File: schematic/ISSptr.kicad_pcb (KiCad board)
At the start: 2 copper layers, 31 parts, among them J1 TYPE-C-31-M-12, J2 PROG, J3 B5B-XH-A, J4 Servo, Q1 BC817, Q2 BC817, U1 AMS1117-3.3, U2 ESP-WROOM-32, U3 HMC5883L-TR, U4 ULN2003AD

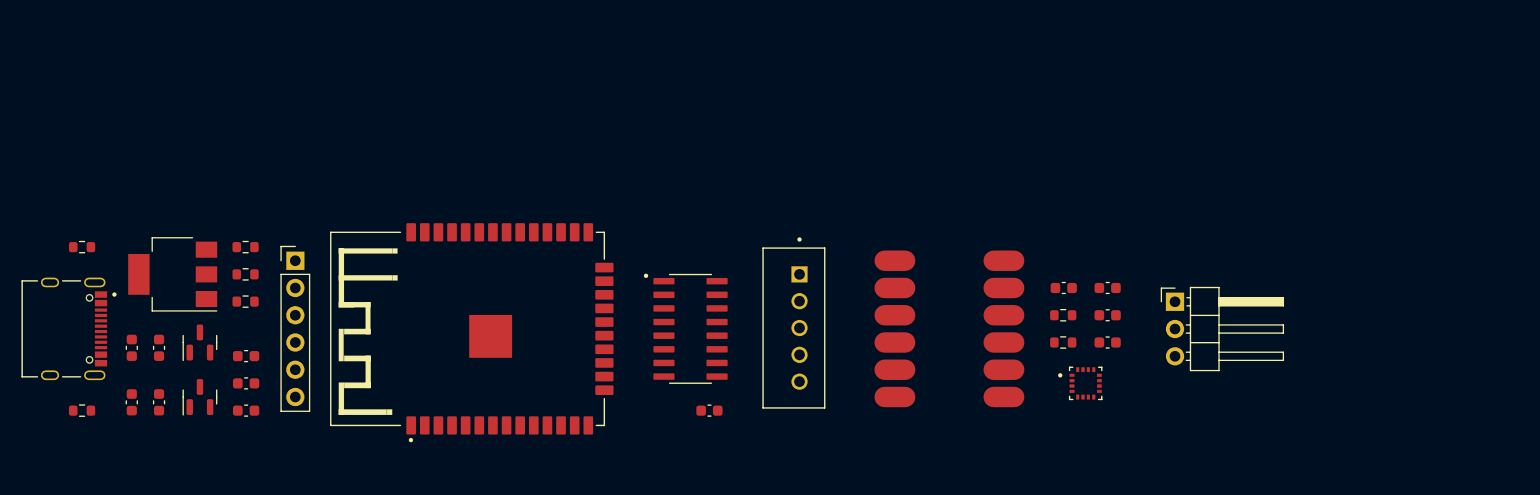
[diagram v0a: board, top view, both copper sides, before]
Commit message: Remove component outlines on silkscreen
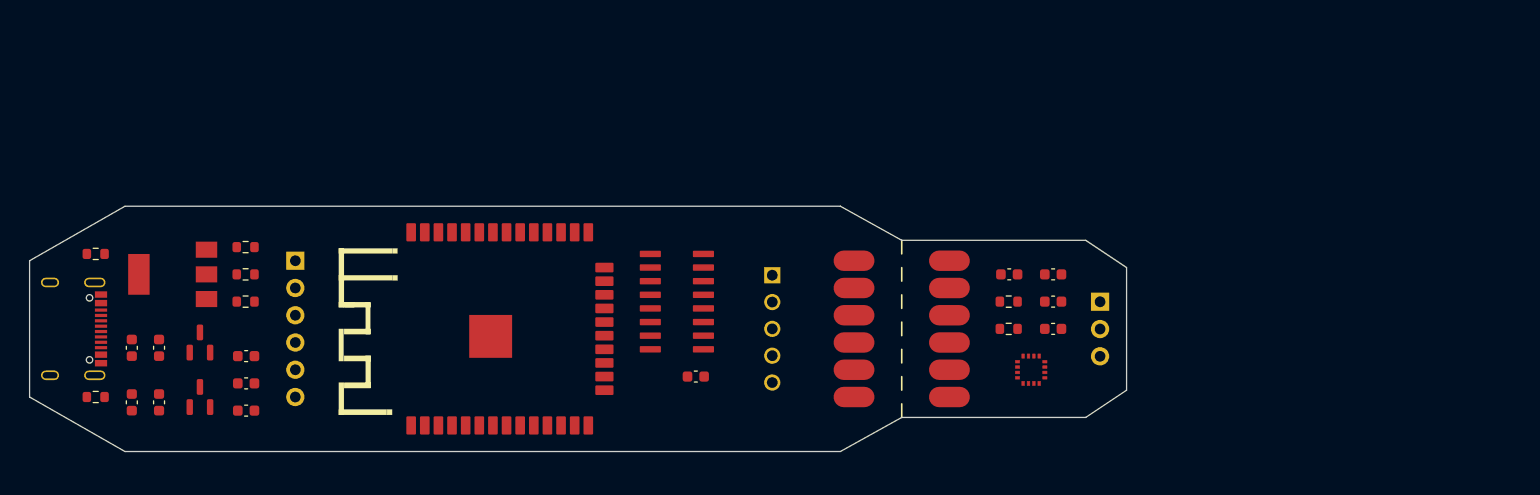
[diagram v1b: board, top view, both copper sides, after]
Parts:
- moved J4 6.98 mm to (157.6, 99.1)
- moved R7 5.24 mm to (149.0, 101.6)
- moved U3 5.24 mm to (151.1, 105.4)
- moved R6 5.24 mm to (149.0, 99.1)
- moved C10 5.24 mm to (153.2, 101.6)
- moved C11 5.24 mm to (149.1, 96.5)
- moved C8 5.24 mm to (153.2, 96.5)
- moved C9 5.24 mm to (153.2, 99.1)
- moved J6 5.08 mm to (143.5, 101.6)
- moved J5 3.81 mm to (134.6, 101.6)
- moved C12 3.42 mm to (119.9, 106.0)
- moved U4 2.84 mm to (118.1, 99.1)
- moved J3 2.54 mm to (126.5, 101.6)
- moved R2 1.80 mm to (63.9, 108.0)
- moved R1 1.42 mm to (63.9, 94.6)
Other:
- board outline added: 102.2 x 22.9 mm

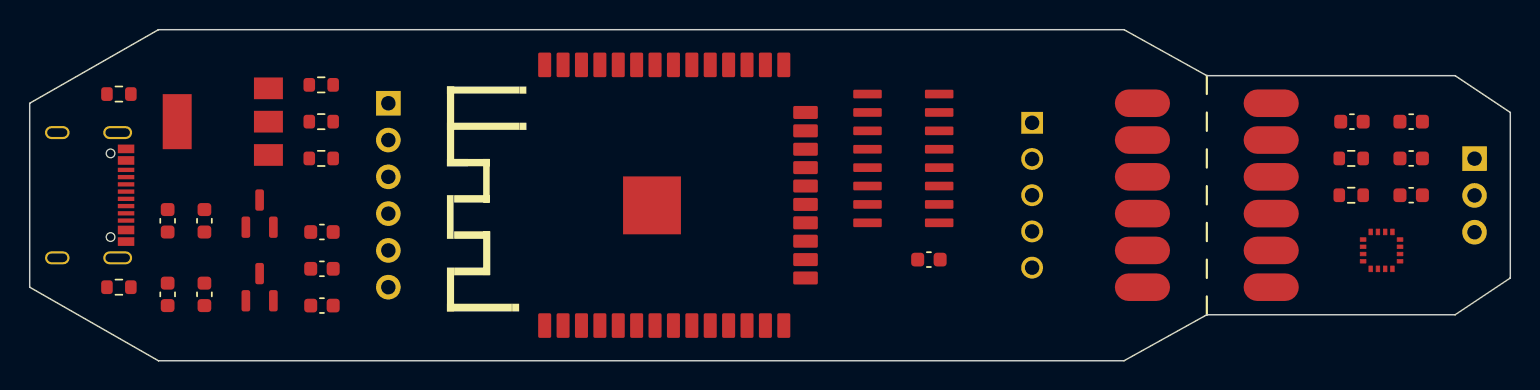
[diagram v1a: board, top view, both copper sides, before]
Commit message: Trace PCB
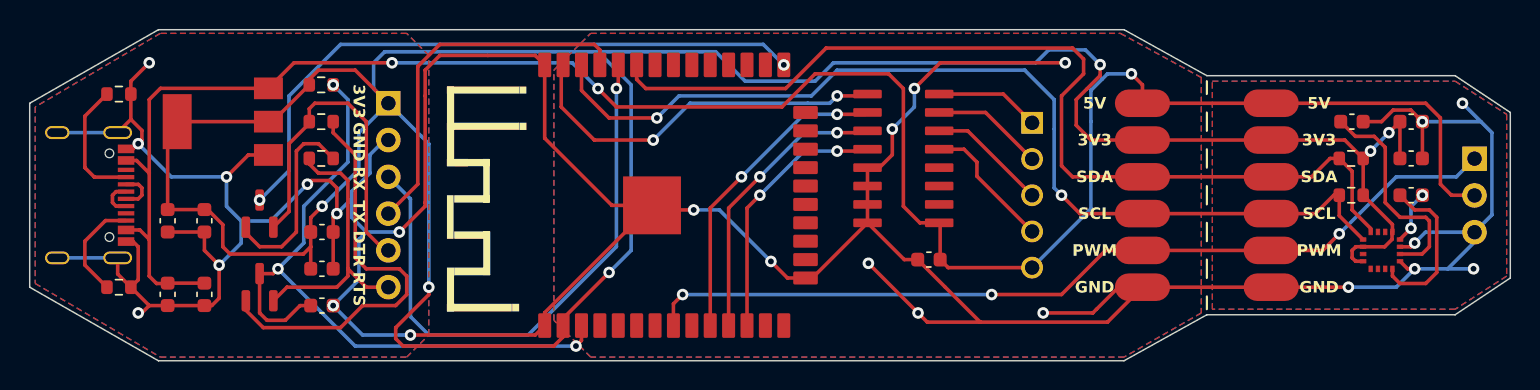
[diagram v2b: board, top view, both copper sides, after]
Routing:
- net GND: track 0.00 -> 286.1 mm, vias 0 -> 24
- net +3.3V: track 0.00 -> 200.9 mm, vias 0 -> 6
- net +5V: track 0.00 -> 143.8 mm, vias 0 -> 3
- net /Compass/SCL: track 0.00 -> 68.2 mm, vias 0 -> 2
- net /Compass/SDA: track 0.00 -> 67.6 mm
- net /ESP32/SERVO: track 0.00 -> 61.0 mm, vias 0 -> 3
- net Net-(Q1-C): track 0.00 -> 47.8 mm, vias 0 -> 3
- net Net-(Q2-C): track 0.00 -> 44.3 mm, vias 0 -> 2
- net /ESP32/PROG_RX: track 0.00 -> 40.2 mm, vias 0 -> 1
- net Net-(Q1-B): track 0.00 -> 28.6 mm
- net /ESP32/STEPPER_A: track 0.00 -> 26.4 mm, vias 0 -> 2
- net /ESP32/PROG_TX: track 0.00 -> 25.4 mm
- net /ESP32/PROG_DTR: track 0.00 -> 23.5 mm
- net /ESP32/STEPPER_B: track 0.00 -> 21.7 mm, vias 0 -> 2
- net /ESP32/STEPPER_C: track 0.00 -> 19.9 mm, vias 0 -> 2
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- added copper zone on B.Cu, net GND
- added copper zone on F.Cu, net GND
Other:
- board text added: "3V3"
- board text added: "5V"
- board text added: "DTR"
- board text added: "GND"
- board text added: "PWM"
- board text added: "RTS"
- board text added: "RX"
- board text added: "SCL"
- board text added: "SDA"
- board text added: "TX"
- board text added: "made with <3 in prague"

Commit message: Setup PCB for production
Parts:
- moved C11 32.6 mm to (181.7, 96.5)
- moved C12 32.6 mm to (152.5, 106.0)
- moved C2 32.6 mm to (102.4, 108.4)
- moved C3 32.6 mm to (102.4, 103.4)
- moved J1 32.6 mm to (92.3, 101.6)
- moved J2 32.6 mm to (115.1, 95.2)
- moved J3 32.6 mm to (159.1, 101.6)
- moved J5 32.6 mm to (167.2, 101.6)
- moved J6 32.6 mm to (176.1, 101.6)
- moved Q1 32.6 mm to (106.2, 108.0)
- moved Q2 32.6 mm to (106.2, 102.9)
- moved R6 32.6 mm to (181.6, 99.1)
- moved R7 32.6 mm to (181.6, 101.6)
- moved U2 32.6 mm to (134.2, 101.6)
- moved U3 32.6 mm to (183.7, 105.4)
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
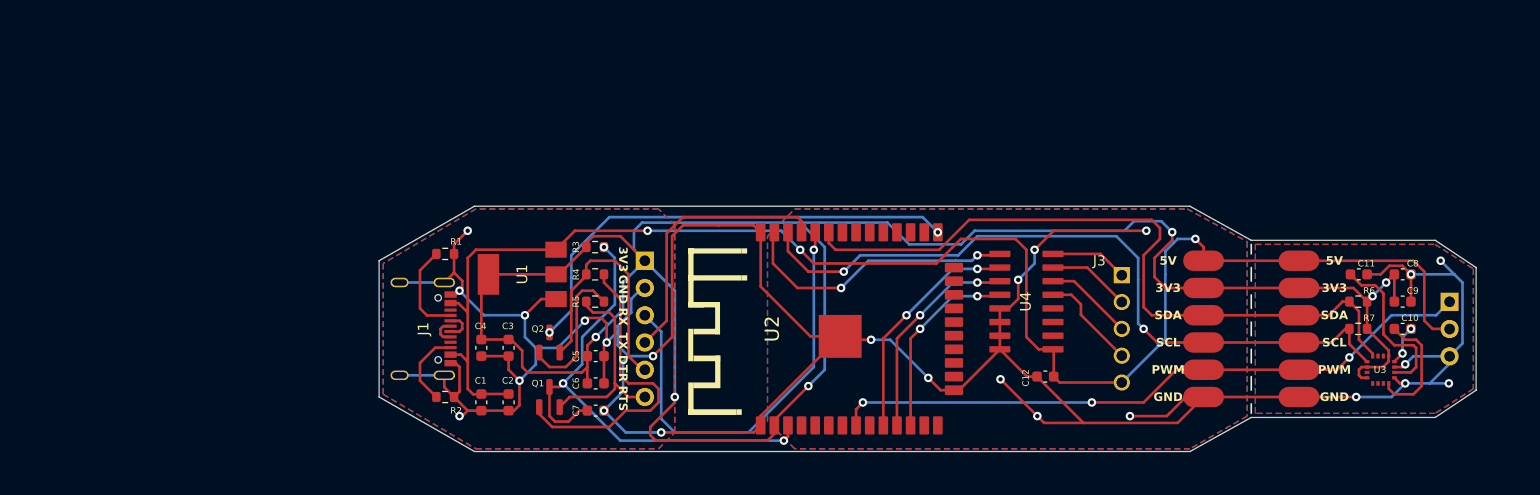
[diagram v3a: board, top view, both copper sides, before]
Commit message: Reduce PCB footprint
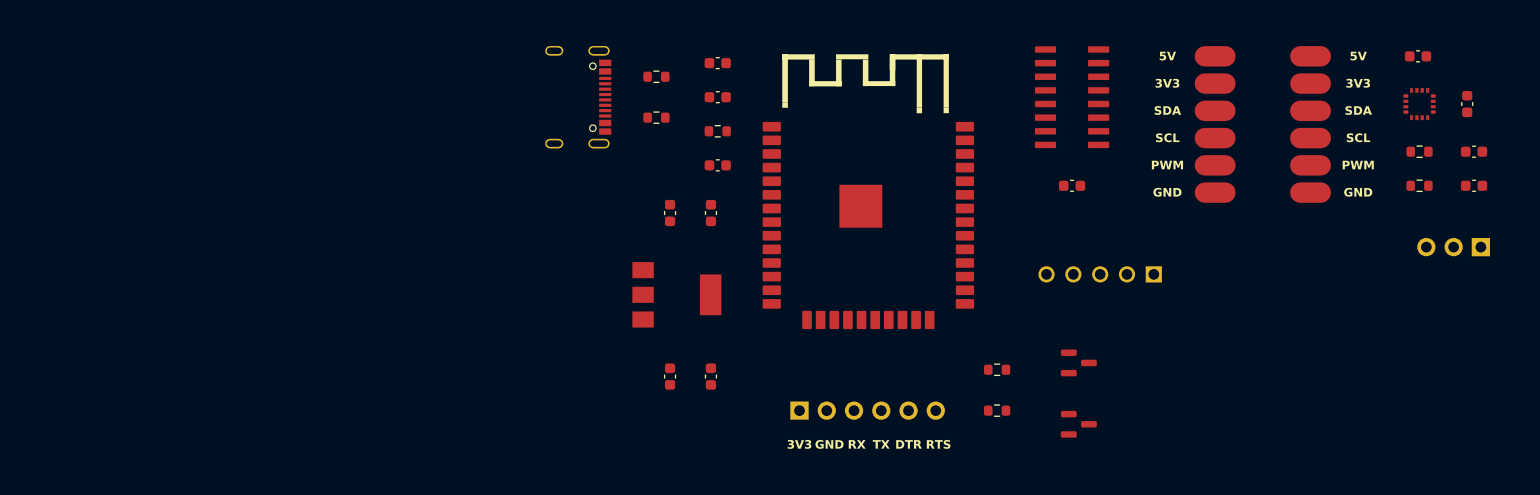
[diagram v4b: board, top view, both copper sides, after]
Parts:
- moved Q2 49.9 mm to (155.6, 110.5), turned to 0 degrees
- moved Q1 49.4 mm to (155.6, 104.8), turned to 0 degrees
- moved R4 39.6 mm to (148.0, 109.2)
- moved R5 38.0 mm to (148.0, 105.4)
- moved R2 32.6 mm to (116.2, 81.9)
- moved C6 31.9 mm to (121.9, 76.8)
- moved C5 26.7 mm to (121.9, 80.0)
- moved J1 26.0 mm to (106.7, 80.0)
- moved C2 25.8 mm to (121.3, 90.8)
- moved R1 25.7 mm to (116.2, 78.1)
- moved C7 25.5 mm to (121.9, 86.4), turned to 180 degrees
- moved C10 25.4 mm to (187.2, 76.2), turned to 0 degrees
- moved U3 25.0 mm to (187.3, 80.6), turned to 90 degrees
- moved C1 24.9 mm to (117.5, 90.8)
- moved C4 21.6 mm to (121.3, 106.0)
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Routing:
- net GND: track 286.1 -> 0.00 mm, vias 24 -> 0
- net +3.3V: track 200.9 -> 0.00 mm, vias 6 -> 0
- net +5V: track 143.8 -> 0.00 mm, vias 3 -> 0
- net /Compass/SCL: track 68.2 -> 0.00 mm, vias 2 -> 0
- net /Compass/SDA: track 67.6 -> 0.00 mm
- net /ESP32/SERVO: track 61.0 -> 0.00 mm, vias 3 -> 0
- net Net-(Q1-C): track 47.8 -> 0.00 mm, vias 3 -> 0
- net Net-(Q2-C): track 44.3 -> 0.00 mm, vias 2 -> 0
- net /ESP32/PROG_RX: track 40.2 -> 0.00 mm, vias 1 -> 0
- net Net-(Q1-B): track 28.6 -> 0.00 mm
- net /ESP32/STEPPER_A: track 26.4 -> 0.00 mm, vias 2 -> 0
- net /ESP32/PROG_TX: track 25.4 -> 0.00 mm
- net /ESP32/PROG_DTR: track 23.5 -> 0.00 mm
- net /ESP32/STEPPER_B: track 21.7 -> 0.00 mm, vias 2 -> 0
- net /ESP32/STEPPER_C: track 19.9 -> 0.00 mm, vias 2 -> 0
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- removed copper zone on B.Cu, net GND
- removed copper zone on F.Cu, net GND
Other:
- board outline removed

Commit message: Route PCB
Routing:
- net +5V: track 0.00 -> 163.5 mm, vias 0 -> 4
- net +3.3V: track 0.00 -> 162.2 mm, vias 0 -> 4
- net /ESP32/SERVO: track 0.00 -> 98.1 mm, vias 0 -> 2
- net /Compass/SDA: track 0.00 -> 51.6 mm, vias 0 -> 2
- net Net-(Q1-C): track 0.00 -> 50.6 mm
- net /Compass/SCL: track 0.00 -> 48.1 mm, vias 0 -> 4
- net /ESP32/STEPPER_D: track 0.00 -> 32.7 mm, vias 0 -> 2
- net /ESP32/STEPPER_C: track 0.00 -> 32.7 mm, vias 0 -> 2
- net /ESP32/STEPPER_B: track 0.00 -> 32.7 mm, vias 0 -> 2
- net /ESP32/PROG_TX: track 0.00 -> 26.3 mm, vias 0 -> 1
- net /ESP32/PROG_RX: track 0.00 -> 26.0 mm, vias 0 -> 1
- net Net-(U4-1C): track 0.00 -> 24.6 mm
- net Net-(U4-2C): track 0.00 -> 23.7 mm
- net Net-(Q2-C): track 0.00 -> 23.6 mm
- net Net-(U4-3C): track 0.00 -> 22.8 mm
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- added copper zone on B.Cu, net GND
- added copper zone on F.Cu, net GND
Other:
- board outline added: 92 x 42 mm
